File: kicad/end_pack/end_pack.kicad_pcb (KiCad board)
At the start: 2 copper layers, 70 x 75 mm, 47 parts, among them J1 cell_+, J10 bal_even_right, J11 bal_odd_right, J12 cell_+, J13 cell_+, J14 bal_odd_right, J15 bal_even_right, J17 communication, J18 communication, J19 communication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

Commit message: gerber + logo
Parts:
- added LOGO1: Logo_Open_Hardware_Small, logo:batpacked-24, B.Cu at (39.9, 70.7)
- added LOGO2: Logo_Open_Hardware_Small, logo:batpacked-24, B.Cu at (60.8, 58.8)
- added LOGO3: Logo_Open_Hardware_Small, logo:batpacked-24, B.Cu at (80.5, 41.9)
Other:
- board text added: "2021"
- board text added: "End Pack, a bat-packed project"
- board text added: "axel"
- board text added: "telec"
- board text added: "william"

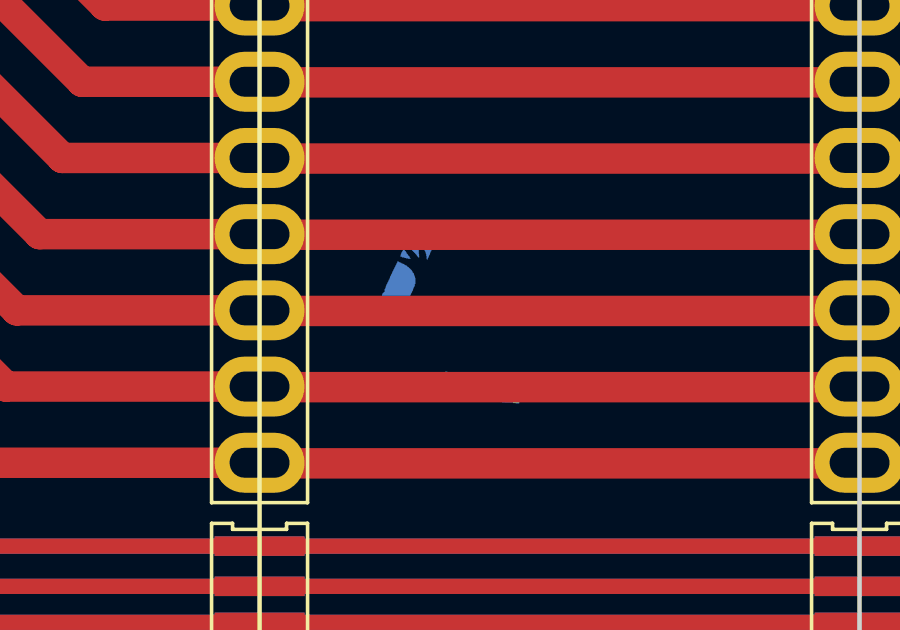
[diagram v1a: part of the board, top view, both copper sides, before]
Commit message: silkscreen correction
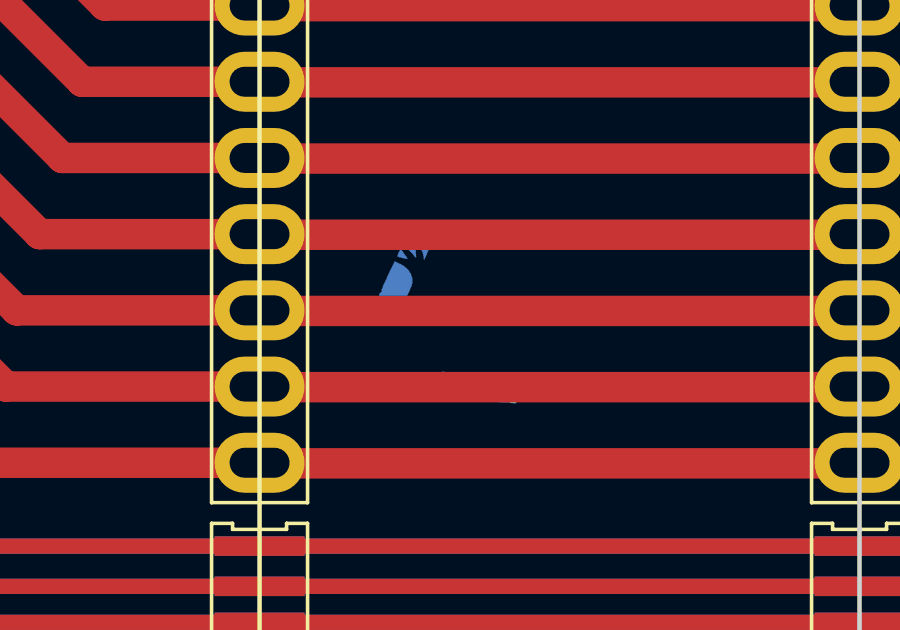
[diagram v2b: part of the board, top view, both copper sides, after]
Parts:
- moved LOGO3 0.10 mm to (80.4, 41.9)

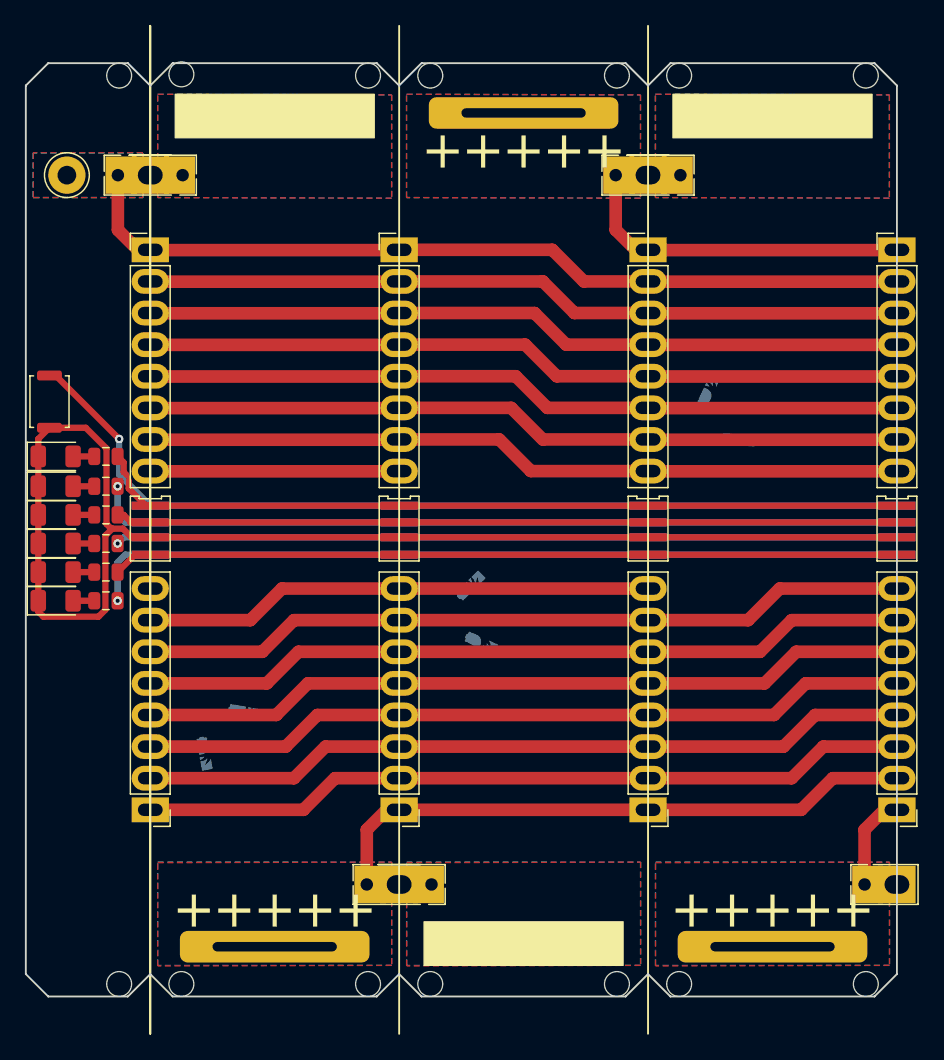
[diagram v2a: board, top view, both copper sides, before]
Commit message: fix silkscreen + hole location
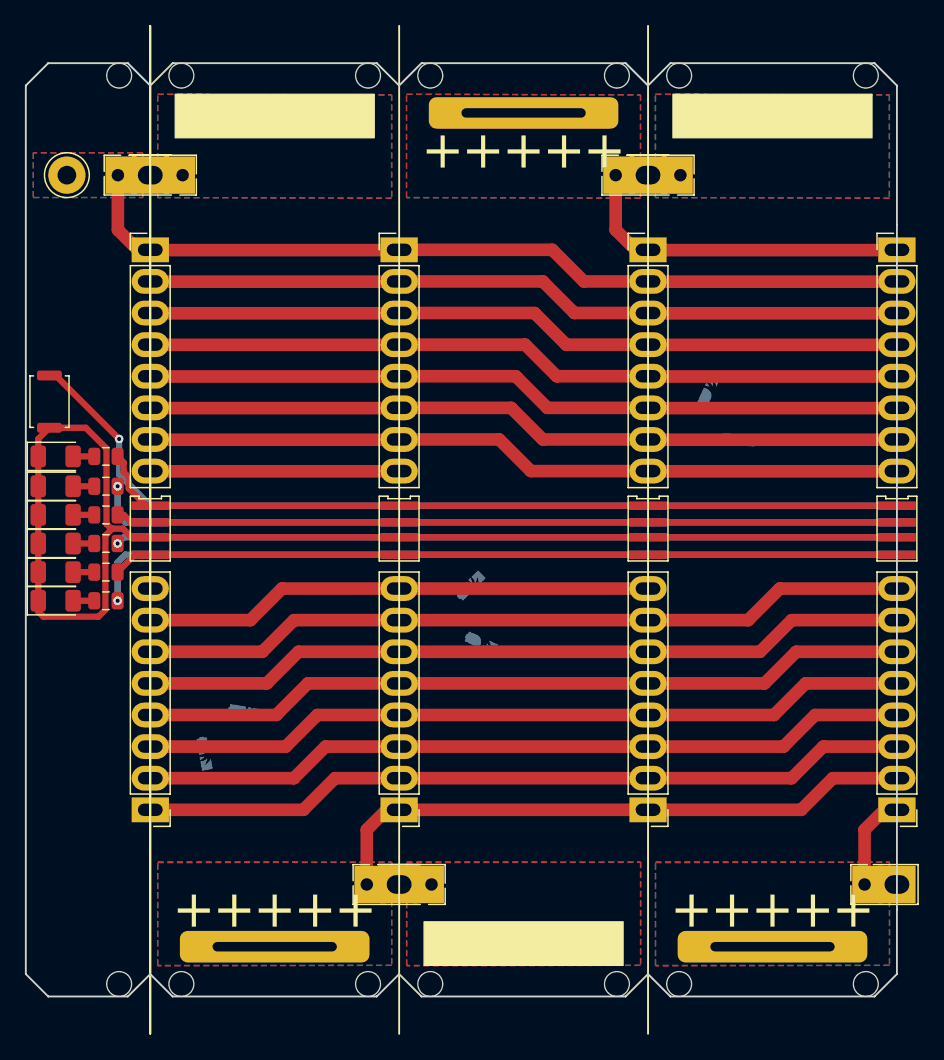
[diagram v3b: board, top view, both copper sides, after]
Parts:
- moved H5 0.10 mm to (34.5, 16.0)
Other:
- outline, holes or cut-outs redrawn
- net class Default: clearance 0.1524 -> 0.127; trace_width 0.1524 -> 0.127
- rule trace_clearance: 0.1524 -> 0.127
- rule trace_min: 0.1524 -> 0.127
- rule via_min_drill: 0.254 -> 0.2
- rule via_min_size: 0.508 -> 0.45
